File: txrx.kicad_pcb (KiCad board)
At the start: 2 copper layers, 41 x 47.5 mm, 3 parts

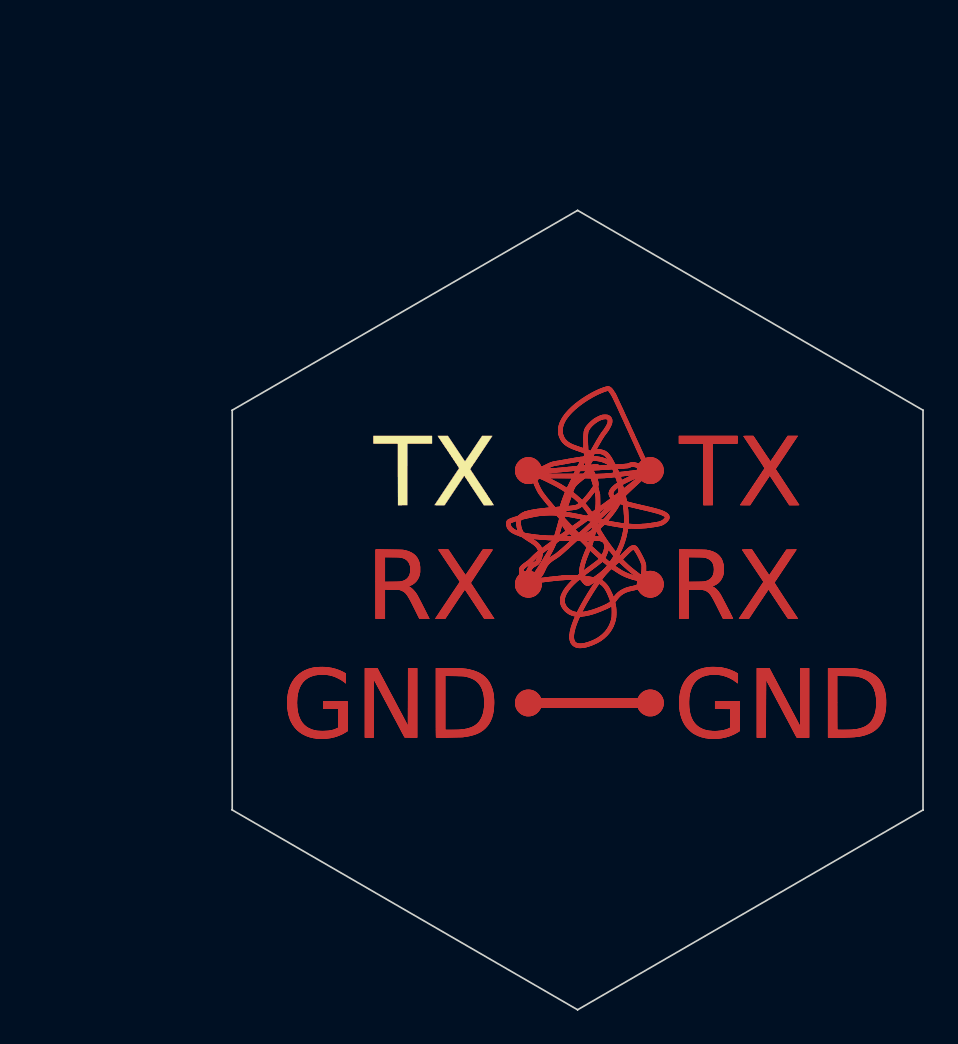
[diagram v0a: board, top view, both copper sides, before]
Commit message: add tx/rx
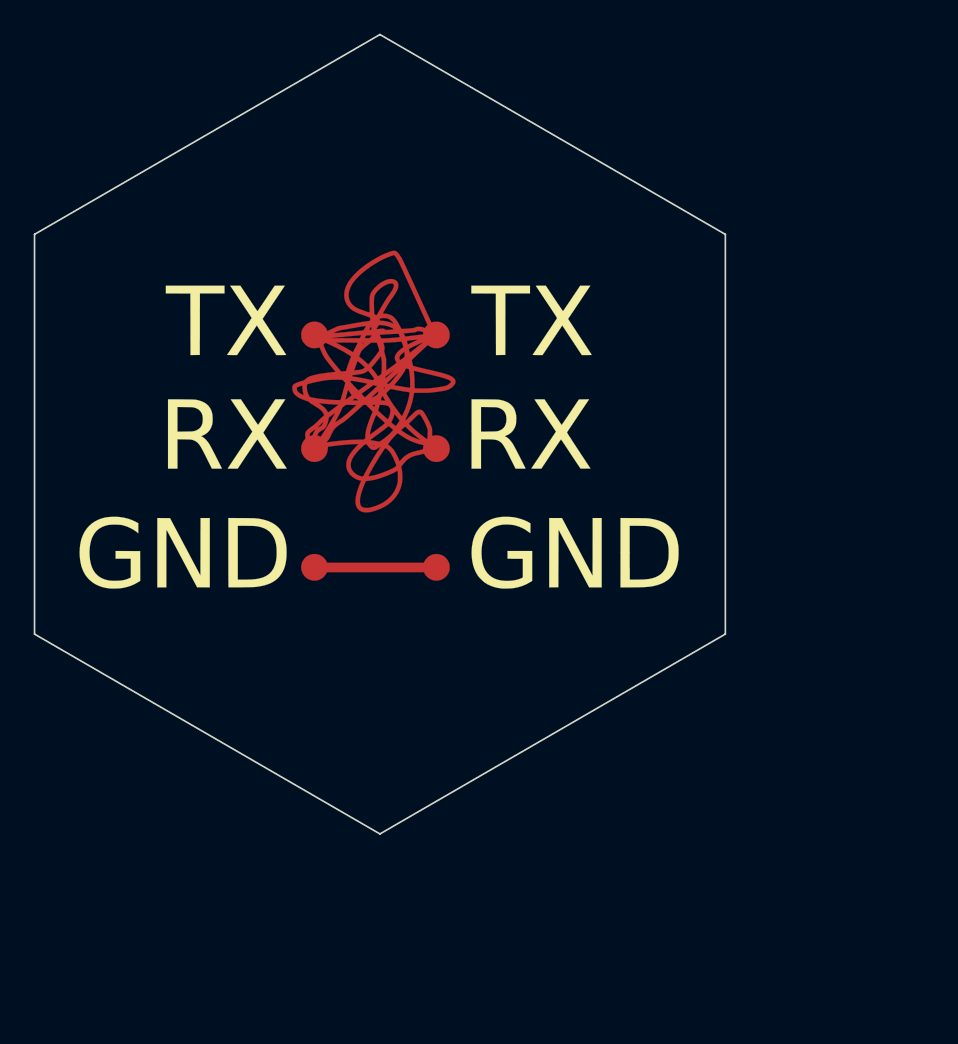
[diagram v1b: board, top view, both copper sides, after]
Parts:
- moved Ref** 15.7 mm to (135.6, 86.1)
- moved Ref** 15.2 mm to (127.4, 85.1)
- moved Ref** 15.0 mm to (127.0, 85.9)

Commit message: add tx/rx
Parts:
- added Ref**: Val**, art:txrx-fail-mask, F.Cu at (127.0, 85.9)

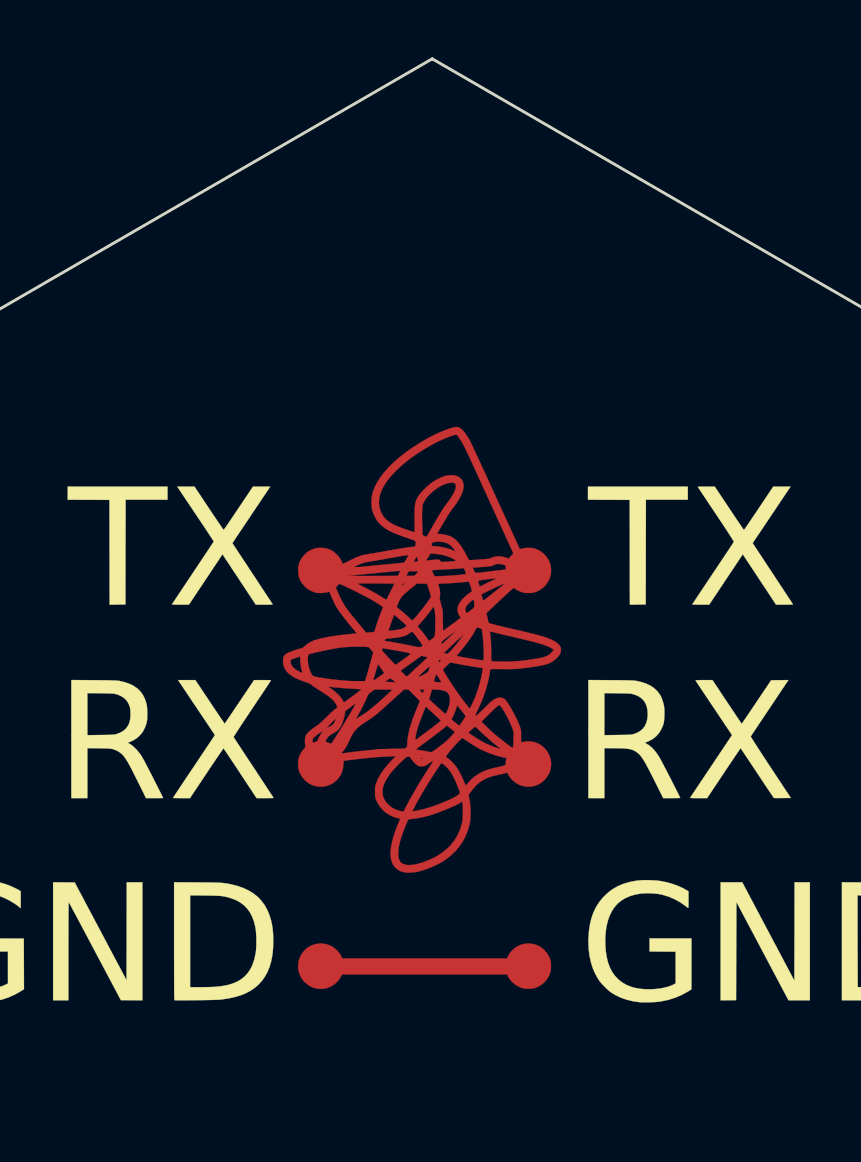
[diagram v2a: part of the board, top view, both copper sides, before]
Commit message: update tx/rx badge
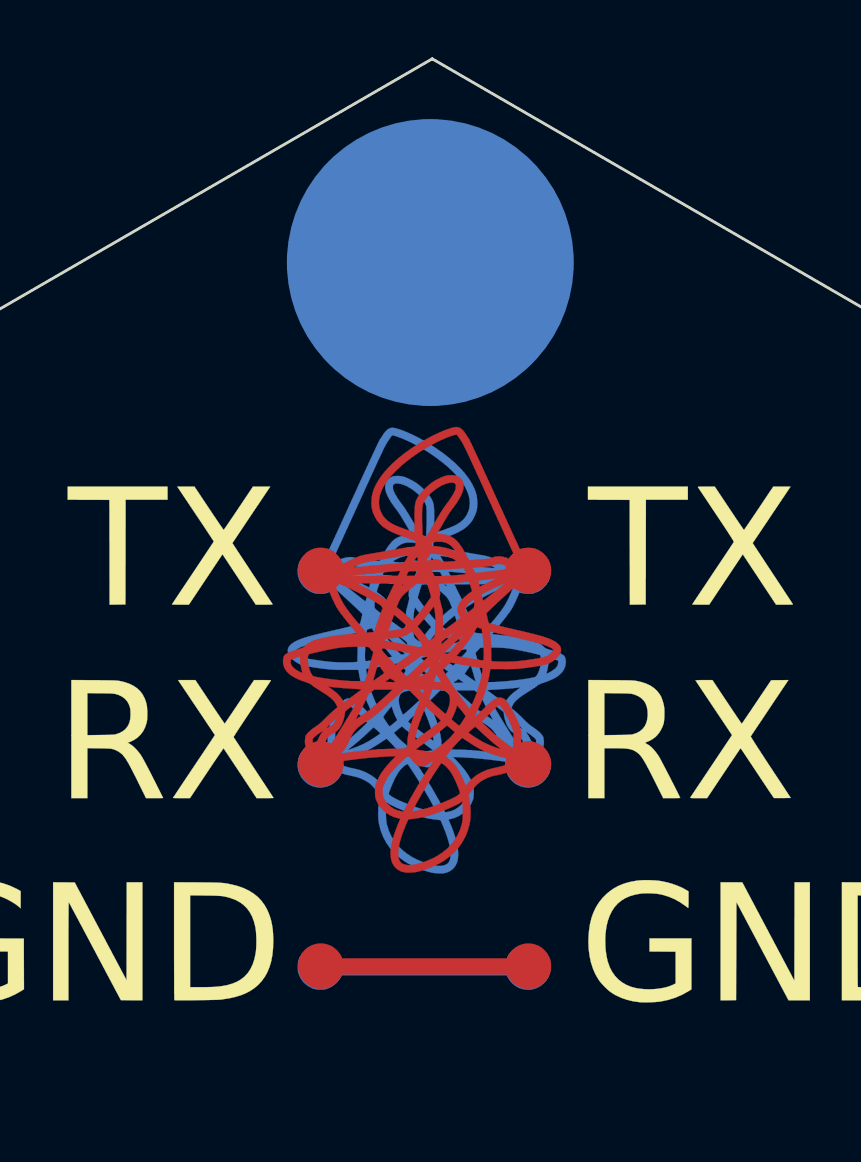
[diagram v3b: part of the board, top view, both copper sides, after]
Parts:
- added REF**: TestPoint_Pad_D4.0mm, TestPoint:TestPoint_Pad_D4.0mm, B.Cu at (131.4, 67.8)
- added Ref**: Val**, art:txrx-fail-mask, B.Cu at (135.4, 86.0)
- added Ref**: Val**, art:txrx-fail-cu, B.Cu at (135.4, 86.0)
- added Ref**: Val**, art:txrx-fail-silk, B.Cu at (135.1, 85.1)
